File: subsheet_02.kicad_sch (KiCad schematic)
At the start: 0 parts

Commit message: CPU : pulled up addr24..addr31 ; CPLD : started
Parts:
- added J301: JTAG+VPP, symbol Connector_Generic:Conn_02x05_Odd_Even
- added NT301: NetTie_2, symbol Device:NetTie_2
- added U301: ATF1508AS_L_100A_TQFP_JTAG_ENABLED_PHY, Package_QFP:TQFP-100_14x14mm_P0.5mm, symbol atf1508as-tqfp100-jtag:ATF1508AS_L_100A_TQFP_JTAG_ENABLED_PHY
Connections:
- new net +3V3: NT301.1
- new net 3V3_CPLD: NT301.2
- new net CPU_R/~{W}: U301.7 (MC27)
- new net FC0: U301.23 (MC37)
- new net FC1: U301.22 (MC38)
- new net FC2: U301.21 (MC40)
- new net IPL0: U301.20 (MC41)
- new net IPL1: U301.19 (MC43)
- new net IPL2: U301.17 (MC45)
- new net ~{CPU_AS}: U301.2 (MC1)
- new net ~{CPU_BERR}: U301.16 (MC46)
- new net ~{CPU_BGACK}: U301.10 (MC22)
- new net ~{CPU_BG}: U301.9 (MC24)
- new net ~{CPU_BR}: U301.12 (MC21)
- new net ~{CPU_DTACK}: U301.8 (MC25)
- new net ~{CPU_HALT}: U301.13 (MC19)
- new net ~{CPU_LDS}: U301.6 (MC29)
- new net ~{CPU_RESET}: U301.14 (MC17)
- new net ~{CPU_UDS}: U301.5 (MC30)

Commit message: Continue CPLD
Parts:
- added C301, C302, C303, C304, C305, C306, C307, C308: 0.22uF, symbol Device:C_Small
- added R301, R302: 4K7, symbol Device:R_Small_US
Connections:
- net 3V3_CPLD: now also U301.18 (VCCIO), U301.3 (VCCIO), U301.34 (VCCIO), U301.39 (VCCINT), U301.51 (VCCIO), U301.66 (VCCIO), U301.82 (VCCIO), U301.91 (VCCINT), C301.1, C302.1, C303.1, C304.1, C305.1, C306.1, C307.1, C308.1, R301.1
- net TMS: now reaches J301.1 (Pin_1)
- net TMS: now also U301.15 (MC48/TMS), R301.2
- net GND: now reaches J301.10 (Pin_10)
- net GND: now also J301.2 (Pin_2), J301.4 (Pin_4), J301.6 (Pin_6), J301.8 (Pin_8), U301.11 (GND), U301.26 (GND), U301.38 (GND), U301.43 (GND), U301.59 (GND), U301.74 (GND), U301.86 (GND), U301.95 (GND), C301.2, C302.2, C303.2, C304.2, C305.2, C306.2, C307.2, C308.2, R302.1
- net TCK: now reaches J301.3 (Pin_3)
- net TCK: now also U301.62 (MC96/TCK), R302.2
- net TDI: now reaches J301.5 (Pin_5)
- net TDI: now also U301.4 (MC32/TDI)
- net TDO: now reaches J301.7 (Pin_7)
- net TDO: now also U301.73 (MC112/TDO)
- net VPP: now reaches J301.9 (Pin_9)
- net VPP: now also U301.88 (OE1/VPP)
- net A31: now reaches U301.24 (MC35)
- net A30: now reaches U301.25 (MC33)
- net A29: now reaches U301.27 (MC64)
- net A28: now reaches U301.28 (MC62)
- net A27: now reaches U301.29 (MC61)
- net A26: now reaches U301.30 (MC59)
- net A25: now reaches U301.31 (MC57)
- net A24: now reaches U301.32 (MC56)
- net A23: now reaches U301.33 (MC54)
- net A22: now reaches U301.35 (MC53)
- net A21: now reaches U301.36 (MC51)
- net A20: now reaches U301.37 (MC49)
- net A19: now reaches U301.40 (MC65)
- net A18: now reaches U301.42 (MC69)
- net A17: now reaches U301.44 (MC70)
- net A16: now reaches U301.45 (MC72)
- net A15: now reaches U301.46 (MC73)
- net A14: now reaches U301.47 (MC75)
- net A13: now reaches U301.48 (MC77)
- net A12: now reaches U301.49 (MC78)
- net A11: now reaches U301.50 (MC80)
- net A10: now reaches U301.52 (MC81)
- net A9: now reaches U301.53 (MC83)
- net A8: now reaches U301.54 (MC85)
- net D0: now reaches U301.55 (MC86)
- net D1: now reaches U301.56 (MC88)
- net D2: now reaches U301.57 (MC89)
- net D3: now reaches U301.58 (MC91)
- net D4: now reaches U301.60 (MC93)
- net D5: now reaches U301.61 (MC94)
- net D6: now reaches U301.63 (MC97)
- net D7: now reaches U301.64 (MC99)
- net CPLD_CLOCK: now reaches U301.87 (GCLK1)
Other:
- moved on the sheet: J301

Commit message: Almost done with CPLD
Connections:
- net CDPL_FPGA_CS: now reaches U301.100 (MC5)
- net ROM2: now reaches U301.65 (MC101)
- net ROM3: now reaches U301.67 (MC102)
- net ROM4: now reaches U301.68 (MC104)
- net CPLD_MFP_CS: now reaches U301.69 (MC105)
- net CPLD_IRQ_IDE: now reaches U301.97 (MC9)
- net CPLD_IRQ_MIDI: now reaches U301.98 (MC8)
- net CPLD_IRQ_HID: now reaches U301.99 (MC6)
- no-connect marks 0 -> 18
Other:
- note added: "Cartridge ROM (2 signals)"
- note added: "From FPGA module"
- note added: "ROM (1 MiB)"
- note added: "TODO : * what to do for GCLR, PD1, PD2 ?"

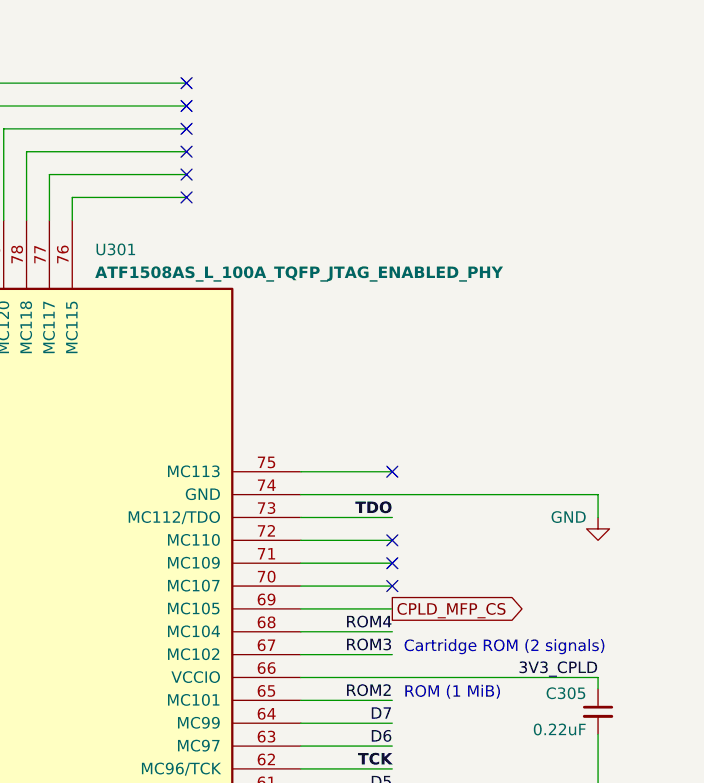
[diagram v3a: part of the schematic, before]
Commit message: Start MFP, with builtin RSVE mod
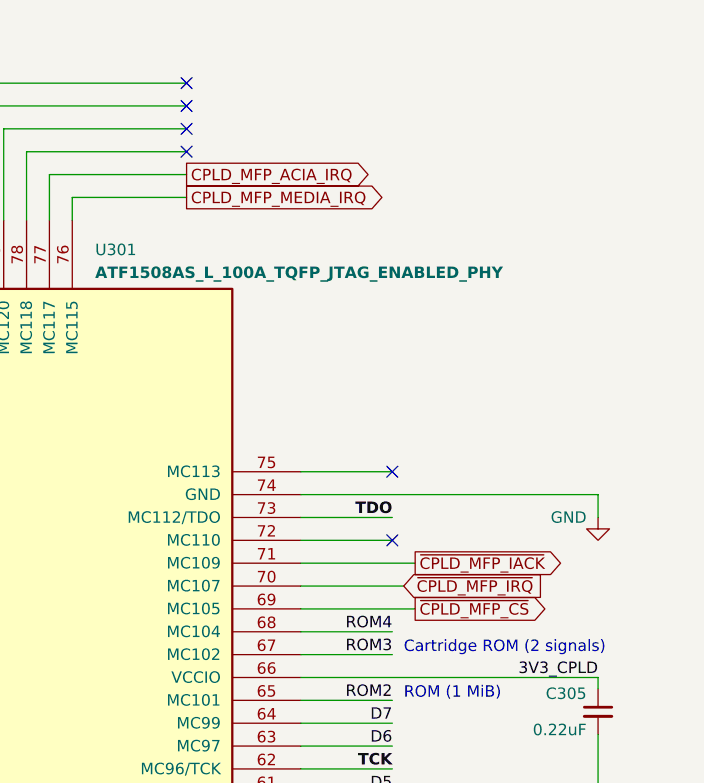
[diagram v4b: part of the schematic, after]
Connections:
- net ~{CPLD_MFP_IRQ}: now reaches U301.70 (MC107)
- net ~{CPLD_MFP_IACK}: now reaches U301.71 (MC109)
- net CPLD_MFP_MEDIA_IRQ: now reaches U301.76 (MC115)
- net CPLD_MFP_ACIA_IRQ: now reaches U301.77 (MC117)
- net CPLD_MFP_CS renamed ~{CPLD_MFP_CS}
- no-connect marks 18 -> 14
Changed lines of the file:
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@@
   (no_connect (at 147.32 53.34))
   (no_connect (at 111.76 53.34))
-  (no_connect (at 147.32 58.42))
   (no_connect (at 88.9 52.07))
   (no_connect (at 93.98 52.07))
   (no_connect (at 147.32 55.88))
-  (no_connect (at 170.18 101.6))
   (no_connect (at 170.18 99.06))
-  (no_connect (at 147.32 60.96))
-  (no_connect (at 170.18 104.14))
   (no_connect (at 116.84 53.34))
   (no_connect (at 114.3 53.34))
@@
     (stroke (width 0) (type default))
   )
+  (wire (pts (xy 160.02 104.14) (xy 171.45 104.14))
+    (stroke (width 0) (type default))
+  )
   (wire (pts (xy 173.99 223.52) (xy 173.99 226.06))
     (stroke (width 0) (type default))
@@
     (stroke (width 0) (type default))
   )
-  (wire (pts (xy 160.02 101.6) (xy 170.18 101.6))
-    (stroke (width 0) (type default))
-  )
   (wire (pts (xy 121.92 48.26) (xy 147.32 48.26))
     (stroke (width 0) (type default))
@@
     (stroke (width 0) (type default))
   )
-  (wire (pts (xy 160.02 104.14) (xy 170.18 104.14))
-    (stroke (width 0) (type default))
-  )
   (wire (pts (xy 132.08 185.42) (xy 132.08 175.26))
     (stroke (width 0) (type default))
@@
     (stroke (width 0) (type default))
   )
-  (wire (pts (xy 160.02 106.68) (xy 170.18 106.68))
+  (wire (pts (xy 160.02 106.68) (xy 172.72 106.68))
     (stroke (width 0) (type default))
   )
@@
   )
   (wire (pts (xy 193.04 132.08) (xy 193.04 120.65))
+    (stroke (width 0) (type default))
+  )
+  (wire (pts (xy 160.02 101.6) (xy 172.72 101.6))
     (stroke (width 0) (type default))
   )
@@
     )
   )
+  (global_label "~{CPLD_MFP_IRQ}" (shape input) (at 171.45 104.14 0) (fields_autoplaced)
+    (effects (font (size 1.27 1.27)) (justify left))
+    (property "Intersheetrefs" "${INTERSHEET_REFS}" (at 188.2238 104.14 0)
+      (effects (font (size 1.27 1.27)) (justify left) hide)
+    )
+  )
   (global_label "CPLD_CLOCK" (shape input) (at 106.68 53.34 90) (fields_autoplaced)
     (effects (font (size 1.27 1.27)) (justify left))
@@
     )
   )
+  (global_label "~{CPLD_MFP_IACK}" (shape output) (at 172.72 101.6 0) (fields_autoplaced)
+    (effects (font (size 1.27 1.27)) (justify left))
+    (property "Intersheetrefs" "${INTERSHEET_REFS}" (at 190.5219 101.6 0)
+      (effects (font (size 1.27 1.27)) (justify left) hide)
+    )
+  )
   (global_label "~{CPU_BG}" (shape input) (at 38.1 111.76 180) (fields_autoplaced)
     (effects (font (size 1.27 1.27)) (justify right))
@@
     )
   )
-  (global_label "CPLD_MFP_CS" (shape output) (at 170.18 106.68 0) (fields_autoplaced)
+  (global_label "CPLD_MFP_MEDIA_IRQ" (shape output) (at 147.32 60.96 0) (fields_autoplaced)
     (effects (font (size 1.27 1.27)) (justify left))
-    (property "Intersheetrefs" "${INTERSHEET_REFS}" (at 186.228 106.68 0)
+    (property "Intersheetrefs" "${INTERSHEET_REFS}" (at 170.6252 60.96 0)
+      (effects (font (size 1.27 1.27)) (justify left) hide)
+    )
+  )
+  (global_label "~{CPLD_MFP_CS}" (shape output) (at 172.72 106.68 0) (fields_autoplaced)
+    (effects (font (size 1.27 1.27)) (justify left))
+    (property "Intersheetrefs" "${INTERSHEET_REFS}" (at 188.768 106.68 0)
       (effects (font (size 1.27 1.27)) (justify left) hide)
     )
@@
       (effects (font (size 1.27 1.27)) (justify left) hide)
     )
+  )
+  (global_label "CPLD_MFP_ACIA_IRQ" (shape output) (at 147.32 58.42 0) (fields_autoplaced)
+    (effects (font (size 1.27 1.27)) (justify left))
+    (property "Intersheetrefs" "${INTERSHEET_REFS}" (at 169.1134 58.42 0)
+      (effects (font (size 1.27 1.27)) (justify left) hide)
+    )
